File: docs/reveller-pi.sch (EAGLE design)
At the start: 21 parts, among them IC100 6581, Q100 IRF9Z24N, T100 BC547, X100 RASPI_BOARD_AB_E0, X101 PG203J, X102 CANTON-POWER

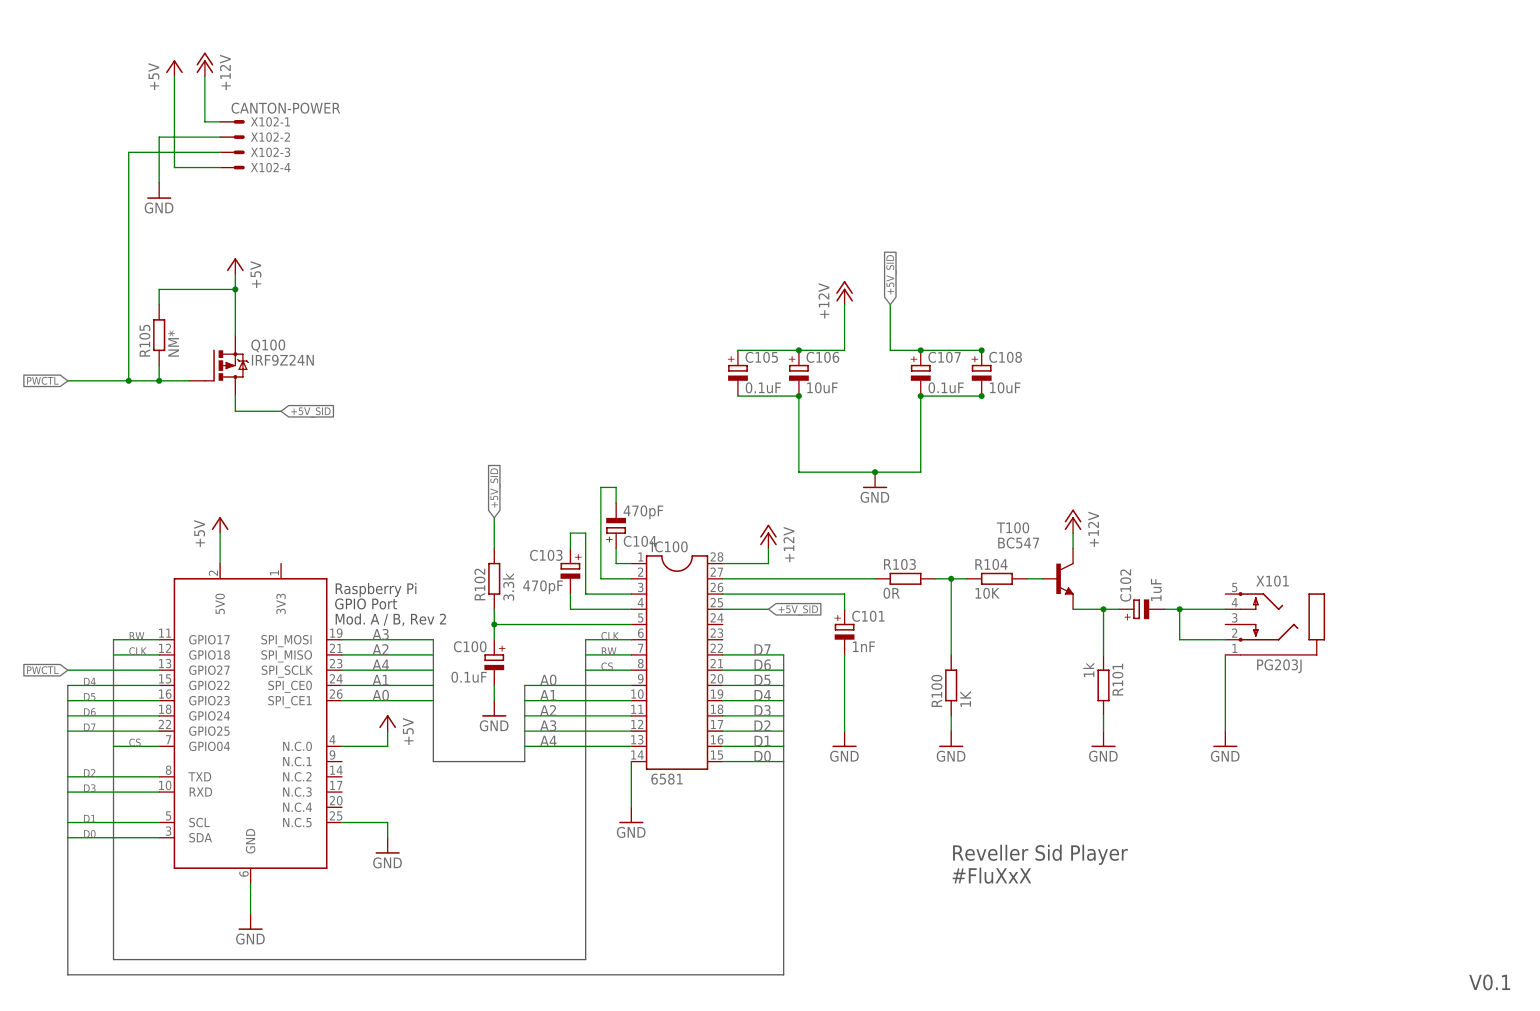
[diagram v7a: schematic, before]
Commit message: Changed from holemounted caps and res to SMDs
Changed to get a better board design, Morten Leikvoll did all of this
because he ment he would look more nice with some of the caps and res.
on the backside og the board.
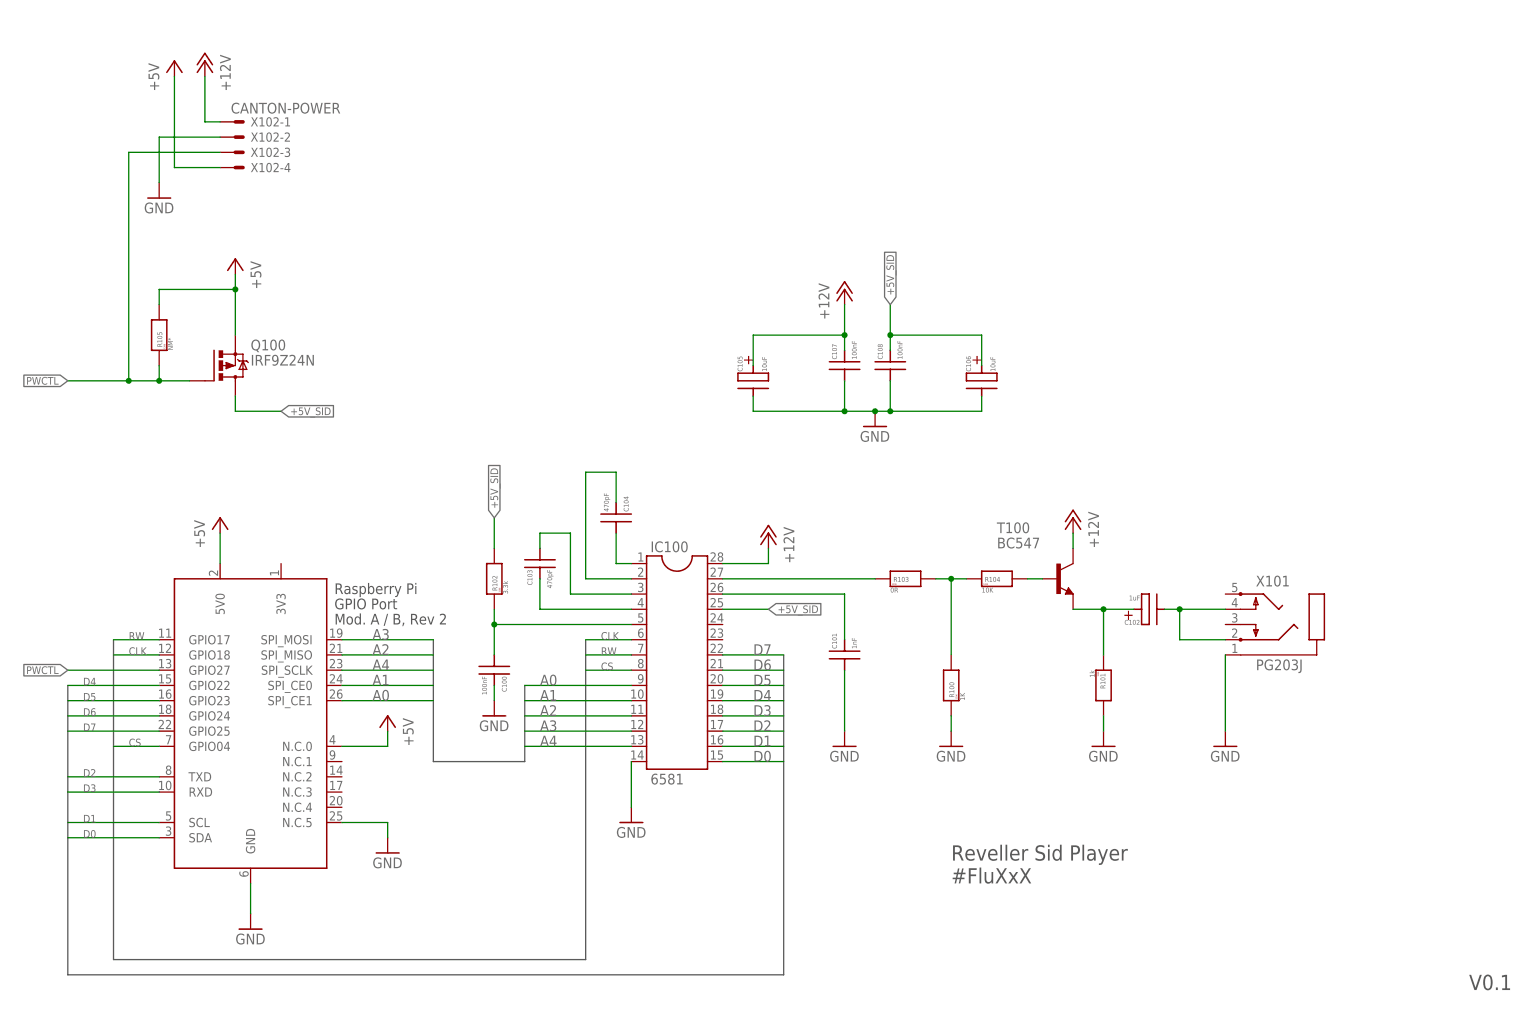
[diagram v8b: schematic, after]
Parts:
- C100, C107: value 0.1uF -> 100nF; device rcl:CPOL-EUE2.5-5 -> cyviz:SMD-IPC_CAPC1206
- C101, C103, C104: device rcl:CPOL-EUE2.5-5 -> cyviz:SMD-IPC_CAPC1206
- C102: device rcl:CPOL-EUE2.5-5 -> cyviz:SMD-IPC_CAPPOLPXE_H
- C105: value 0.1uF -> 10uF; device rcl:CPOL-EUE2.5-5 -> cyviz:SMD-IPC_CAPPOLC7343
- C106: device rcl:CPOL-EUE2.5-5 -> cyviz:SMD-IPC_CAPPOLC7343
- C108: value 10uF -> 100nF; device rcl:CPOL-EUE2.5-5 -> cyviz:SMD-IPC_CAPC1206
- R100, R101, R102, R103, R104, R105: device rcl:R-EU_0204/7 -> cyviz:SMD-IPC_RESR1206
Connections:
- net +12V: now also C107.2; no longer C106.+
- net +5V_SID: now also C106.+, C108.2; no longer C107.+, C108.+
- net CAP1A: now also C104.1; no longer C104.+
- net CAP1B: now also C104.2; no longer C104.-
- net CAP2A: now also C103.1; no longer C103.+
- net CAP2B: now also C103.2; no longer C103.-
- net CAPX: now also C101.2; no longer C101.+
- net GND: now also C100.2, C101.1, C107.1, C108.1; no longer C100.-, C101.-, C107.-, C108.-
- net RESET: now also C100.1; no longer C100.+
